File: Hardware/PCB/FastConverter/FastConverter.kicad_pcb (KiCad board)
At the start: 2 copper layers, 3 parts, among them U1 90DegreePort, U2 90DegreePort, U3 ProMicro

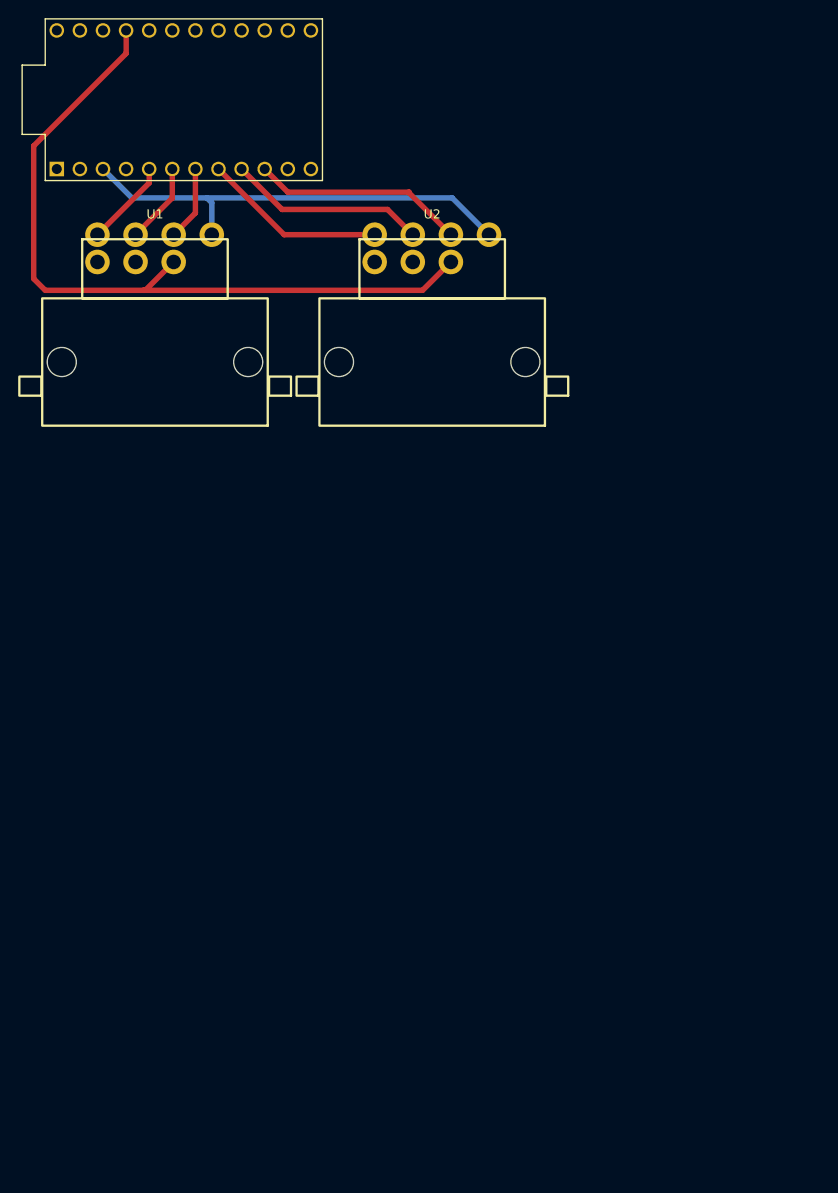
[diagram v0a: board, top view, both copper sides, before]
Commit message: Add circles to edge of board
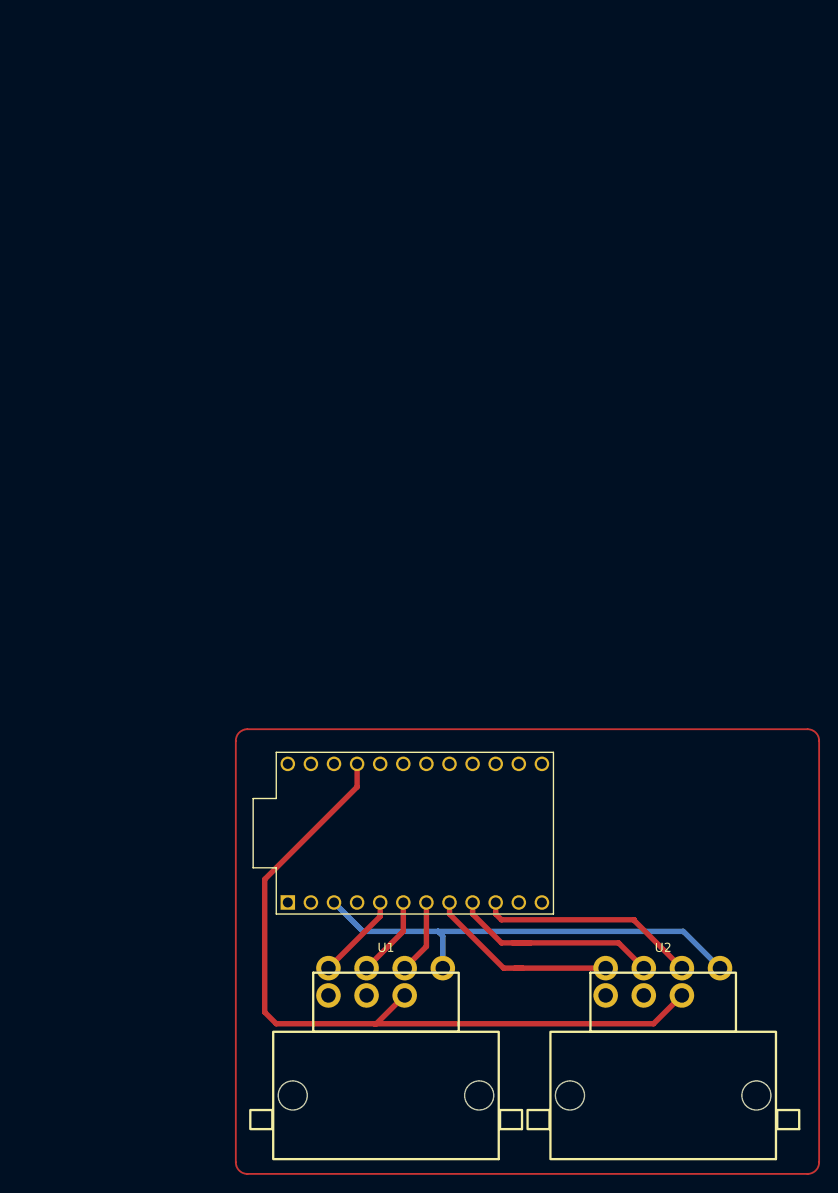
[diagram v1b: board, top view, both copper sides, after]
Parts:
- moved U1 84.6 mm to (99.1, 144.1)
- moved U2 84.6 mm to (129.5, 144.1)
- moved U3 84.6 mm to (102.2, 122.6)
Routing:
- net Net-(U2-PadL): track 21.8 -> 24.5 mm
- net Net-(U2-PadD): track 20.2 -> 21.7 mm
- net Net-(U2-PadC): track 23.5 -> 24.3 mm
